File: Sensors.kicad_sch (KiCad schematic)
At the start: 5 parts, among them U5 LSM6DS3, U6 BMP280

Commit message: V3
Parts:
- removed JP2: SolderJumper_3_Open, Jumper:SolderJumper-3_P1.3mm_Open_RoundedPad1.0x1.5mm, symbol Jumper:SolderJumper_3_Open
- C13: footprint Capacitor_SMD:C_0603_1608Metric_Pad1.08x0.95mm_HandSolder -> Capacitor_SMD:C_0402_1005Metric_Pad0.74x0.62mm_HandSolder
- R16: footprint Resistor_SMD:R_0603_1608Metric_Pad0.98x0.95mm_HandSolder -> Resistor_SMD:R_0402_1005Metric_Pad0.72x0.64mm_HandSolder
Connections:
- net GND: now also U6.5 (SDO)
- no-connect marks 0 -> 2
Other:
- moved on the sheet: R16
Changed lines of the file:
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@@
   (junction (at 40.64 40.64) (diameter 0) (color 0 0 0 0)
   )
-  (junction (at 35.56 50.8) (diameter 0) (color 0 0 0 0)
-  )
   (junction (at 66.04 58.42) (diameter 0) (color 0 0 0 0)
   )
   (junction (at 123.19 29.21) (diameter 0) (color 0 0 0 0)
   )
+  (junction (at 33.02 50.8) (diameter 0) (color 0 0 0 0)
+  )
   (junction (at 66.04 27.94) (diameter 0) (color 0 0 0 0)
   )
@@
   (junction (at 123.19 57.15) (diameter 0) (color 0 0 0 0)
   )
+  (no_connect (at 81.28 35.56))
+  (no_connect (at 81.28 38.1))
   (wire (pts (xy 125.73 29.21) (xy 134.62 29.21))
     (stroke (width 0) (type default) (color 0 0 0 0))
@@
     (stroke (width 0) (type default) (color 0 0 0 0))
   )
-  (wire (pts (xy 106.68 45.72) (xy 113.03 45.72))
-    (stroke (width 0) (type default) (color 0 0 0 0))
-  )
-  (wire (pts (xy 33.02 50.8) (xy 35.56 50.8))
+  (wire (pts (xy 102.87 45.72) (xy 113.03 45.72))
+    (stroke (width 0) (type default) (color 0 0 0 0))
+  )
+  (wire (pts (xy 29.21 50.8) (xy 33.02 50.8))
+    (stroke (width 0) (type default) (color 0 0 0 0))
+  )
+  (wire (pts (xy 102.87 45.72) (xy 102.87 50.8))
     (stroke (width 0) (type default) (color 0 0 0 0))
   )
@@
     (stroke (width 0) (type default) (color 0 0 0 0))
   )
-  (wire (pts (xy 35.56 50.8) (xy 50.8 50.8))
+  (wire (pts (xy 33.02 50.8) (xy 50.8 50.8))
     (stroke (width 0) (type default) (color 0 0 0 0))
   )
@@
     )
   )
-  (global_label "SPI_CS_LSM" (shape input) (at 33.02 50.8 180) (fields_autoplaced)
-    (effects (font (size 1.27 1.27)) (justify right))
-    (property "Intersheet References" "${INTERSHEET_REFS}" (id 0) (at 19.4188 50.7206 0)
+  (global_label "SPI_CS_LSM" (shape input) (at 29.21 50.8 180) (fields_autoplaced)
+    (effects (font (size 1.27 1.27)) (justify right))
+    (property "Intersheet References" "${INTERSHEET_REFS}" (id 0) (at 15.6088 50.7206 0)
       (effects (font (size 1.27 1.27)) (justify right) hide)
     )
@@
     )
     (pin "1")
-  )
-  (symbol (lib_id "Jumper:SolderJumper_3_Open") (at 102.87 45.72 90) (unit 1)
-    (in_bom yes) (on_board yes) (fields_autoplaced)
-    (property "Reference" "JP2" (id 0) (at 100.33 44.4499 90)
-      (effects (font (size 1.27 1.27)) (justify left))
-    )
-    (property "Value" "SolderJumper_3_Open" (id 1) (at 100.33 46.9899 90)
-      (effects (font (size 1.27 1.27)) (justify left) hide)
-    )
-    (property "Footprint" "Jumper:SolderJumper-3_P1.3mm_Open_RoundedPad1.0x1.5mm" (id 2) (at 102.87 45.72 0)
-      (effects (font (size 1.27 1.27)) hide)
-    )
-    (property "Datasheet" "~" (id 3) (at 102.87 45.72 0)
-      (effects (font (size 1.27 1.27)) hide)
-    )
-    (pin "1")
-    (pin "2")
-    (pin "3")
   )
   (symbol (lib_id "power:+3.3V") (at 66.04 25.4 0) (unit 1)
@@
       (effects (font (size 1.27 1.27)) (justify left))
     )
-    (property "Footprint" "Capacitor_SMD:C_0603_1608Metric_Pad1.08x0.95mm_HandSolder" (id 2) (at 135.5852 36.83 0)
+    (property "Footprint" "Capacitor_SMD:C_0402_1005Metric_Pad0.74x0.62mm_HandSolder" (id 2) (at 135.5852 36.83 0)
       (effects (font (size 1.27 1.27)) hide)
     )
@@
     (pin "1")
   )
-  (symbol (lib_id "power:+3.3V") (at 35.56 43.18 0) (unit 1)
-    (in_bom yes) (on_board yes) (fields_autoplaced)
-    (property "Reference" "#PWR0153" (id 0) (at 35.56 46.99 0)
-      (effects (font (size 1.27 1.27)) hide)
-    )
-    (property "Value" "+3.3V" (id 1) (at 35.56 38.1 0))
-    (property "Footprint" "" (id 2) (at 35.56 43.18 0)
-      (effects (font (size 1.27 1.27)) hide)
-    )
-    (property "Datasheet" "" (id 3) (at 35.56 43.18 0)
+  (symbol (lib_id "power:+3.3V") (at 33.02 43.18 0) (unit 1)
+    (in_bom yes) (on_board yes) (fields_autoplaced)
+    (property "Reference" "#PWR0153" (id 0) (at 33.02 46.99 0)
+      (effects (font (size 1.27 1.27)) hide)
+    )
+    (property "Value" "+3.3V" (id 1) (at 33.02 38.1 0))
+    (property "Footprint" "" (id 2) (at 33.02 43.18 0)
+      (effects (font (size 1.27 1.27)) hide)
+    )
+    (property "Datasheet" "" (id 3) (at 33.02 43.18 0)
       (effects (font (size 1.27 1.27)) hide)
     )
@@
     (pin "1")
   )
-  (symbol (lib_id "power:+3.3V") (at 102.87 40.64 0) (unit 1)
-    (in_bom yes) (on_board yes) (fields_autoplaced)
-    (property "Reference" "#PWR0152" (id 0) (at 102.87 44.45 0)
-      (effects (font (size 1.27 1.27)) hide)
-    )
-    (property "Value" "+3.3V" (id 1) (at 102.87 35.56 0))
-    (property "Footprint" "" (id 2) (at 102.87 40.64 0)
-      (effects (font (size 1.27 1.27)) hide)
-    )
-    (property "Datasheet" "" (id 3) (at 102.87 40.64 0)
-      (effects (font (size 1.27 1.27)) hide)
-    )
-    (pin "1")
-  )
-  (symbol (lib_id "Device:R") (at 35.56 46.99 0) (unit 1)
+  (symbol (lib_id "Device:R") (at 33.02 46.99 0) (unit 1)
     (in_bom yes) (on_board yes)
-    (property "Reference" "R16" (id 0) (at 33.02 48.26 90))
-    (property "Value" "10k" (id 1) (at 38.1 48.26 90))
-    (property "Footprint" "Resistor_SMD:R_0603_1608Metric_Pad0.98x0.95mm_HandSolder" (id 2) (at 33.782 46.99 90)
-      (effects (font (size 1.27 1.27)) hide)
-    )
-    (property "Datasheet" "~" (id 3) (at 35.56 46.99 0)
-      (effects (font (size 1.27 1.27)) hide)
-    )
+    (property "Reference" "R16" (id 0) (at 30.48 48.26 90))
+    (property "Value" "10k" (id 1) (at 35.56 48.26 90))
+    (property "Footprint" "Resistor_SMD:R_0402_1005Metric_Pad0.72x0.64mm_HandSolder" (id 2) (at 31.242 46.99 90)
+      (effects (font (size 1.27 1.27)) hide)
+    )
+    (property "Datasheet" "~" (id 3) (at 33.02 46.99 0)
+      (effects (font (size 1.27 1.27)) hide)
+    )

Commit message: Rev 27052023
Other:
- note added: "BMP280"
- note added: "LSM6DS"
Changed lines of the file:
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@@
     (stroke (width 0) (type default) (color 0 0 0 0))
+  )
+  (text "BMP280" (at 99.06 17.78 0)
+    (effects (font (size 1.27 1.27)) (justify left bottom))
+  )
+  (text "LSM6DS" (at 15.24 16.51 0)
+    (effects (font (size 1.27 1.27)) (justify left bottom))
   )
   (global_label "MOSI" (shape input) (at 50.8 45.72 180) (fields_autoplaced)

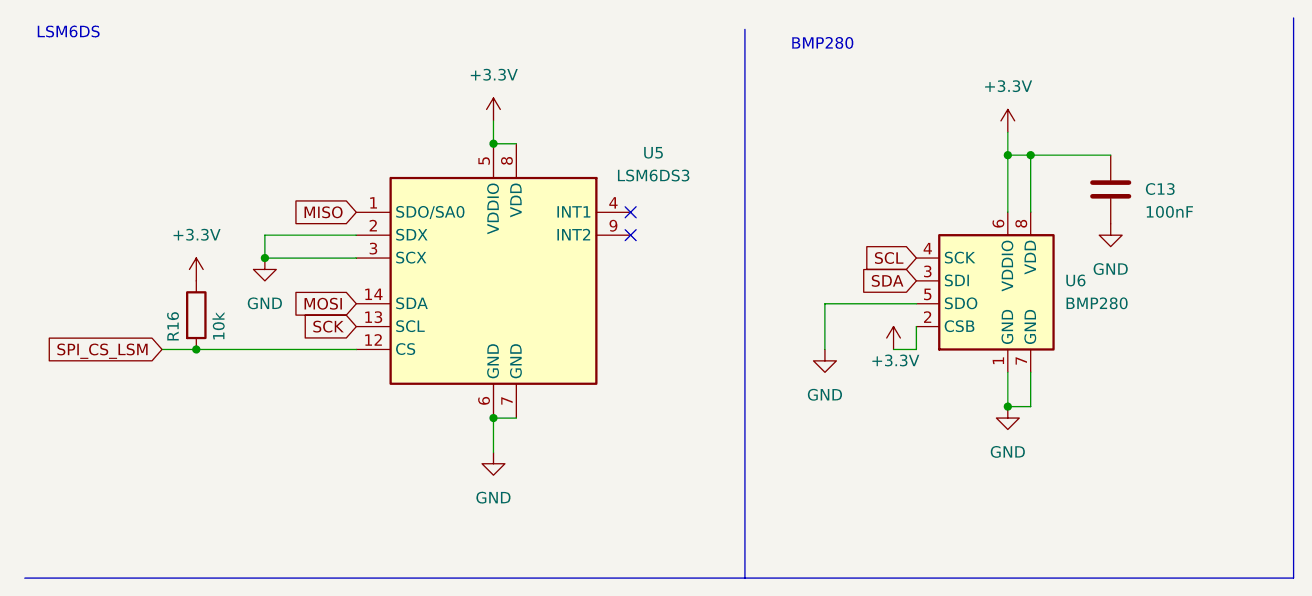
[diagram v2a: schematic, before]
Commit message: Shortcircuit fix, maybe final version before rev2
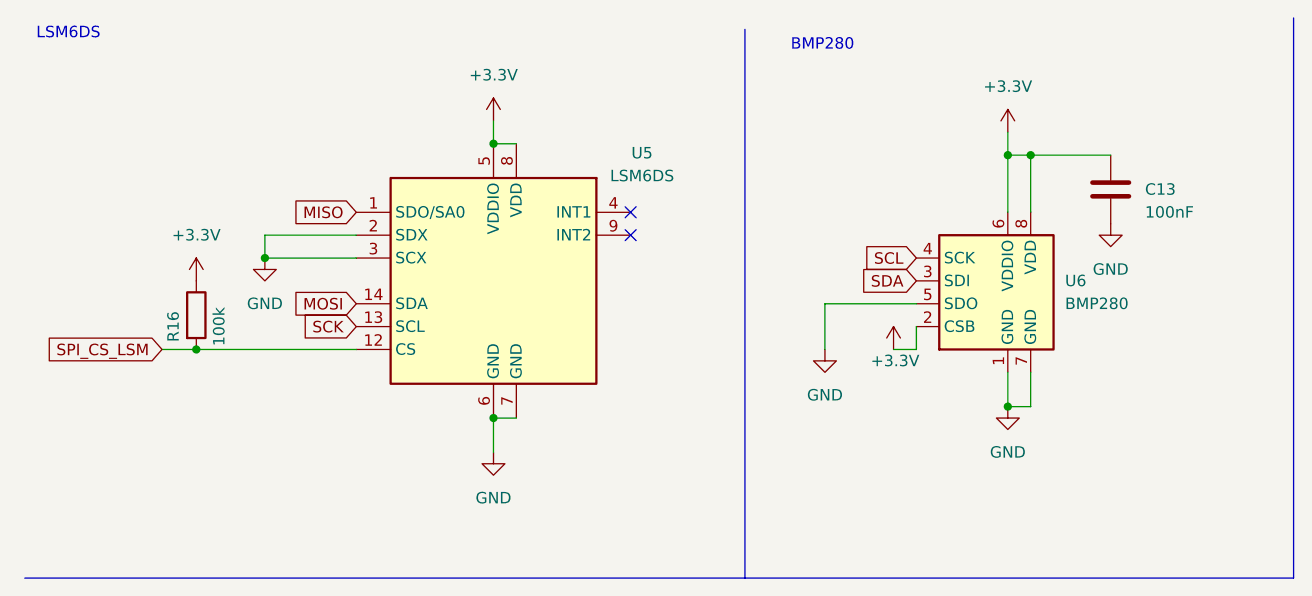
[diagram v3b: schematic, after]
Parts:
- R16: value 10k -> 100k
- U5: value LSM6DS3 -> LSM6DS
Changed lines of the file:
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@@
   (symbol (lib_id "Sensor_Motion:LSM6DS3") (at 66.04 43.18 0) (unit 1)
     (in_bom yes) (on_board yes) (fields_autoplaced)
-    (property "Reference" "U5" (id 0) (at 83.82 28.9812 0))
-    (property "Value" "LSM6DS3" (id 1) (at 83.82 31.5212 0))
+    (property "Reference" "U5" (id 0) (at 82.55 28.9812 0))
+    (property "Value" "LSM6DS" (id 1) (at 82.55 31.5212 0))
     (property "Footprint" "Package_LGA:LGA-14_3x2.5mm_P0.5mm_LayoutBorder3x4y" (id 2) (at 55.88 60.96 0)
       (effects (font (size 1.27 1.27)) (justify left) hide)
@@
     (in_bom yes) (on_board yes)
     (property "Reference" "R16" (id 0) (at 30.48 48.26 90))
-    (property "Value" "10k" (id 1) (at 35.56 48.26 90))
+    (property "Value" "100k" (id 1) (at 35.56 48.26 90))
     (property "Footprint" "Resistor_SMD:R_0402_1005Metric_Pad0.72x0.64mm_HandSolder" (id 2) (at 31.242 46.99 90)
       (effects (font (size 1.27 1.27)) hide)
